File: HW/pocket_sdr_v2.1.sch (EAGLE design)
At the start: 75 parts, among them J1 PIN HEADER 2MM 2P, J2 PIN HEADER 2MM 2P, J3 USB MICRO B RECEPTACLE SMT, J4 SMA JACK EDGE MNT, U1 MAX2771, U2 MAX2771, U3 EZ-USB FX2LP CY7C6813A-56TXC, U4 AT24C128C 8-TSSOP, U5 LDO 3.3V 500mA SOT23-5

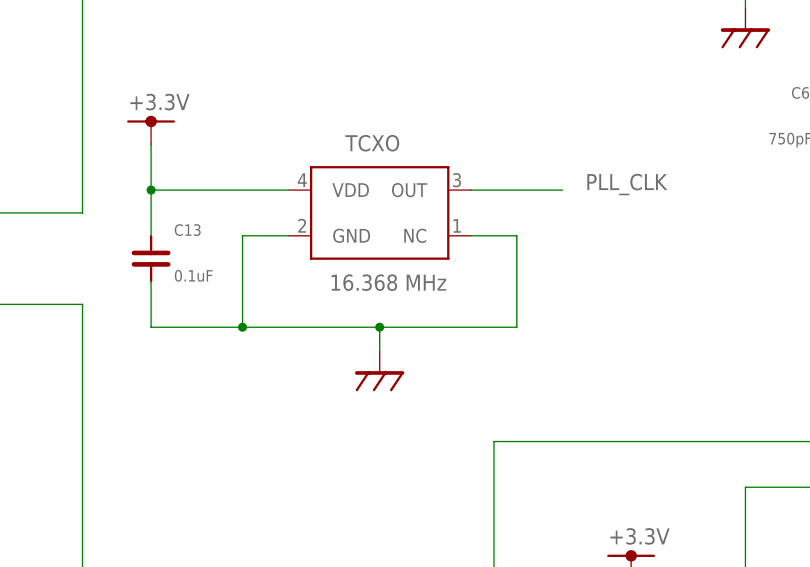
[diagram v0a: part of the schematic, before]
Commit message: TCXO 16.368 -> 24.000 MHz
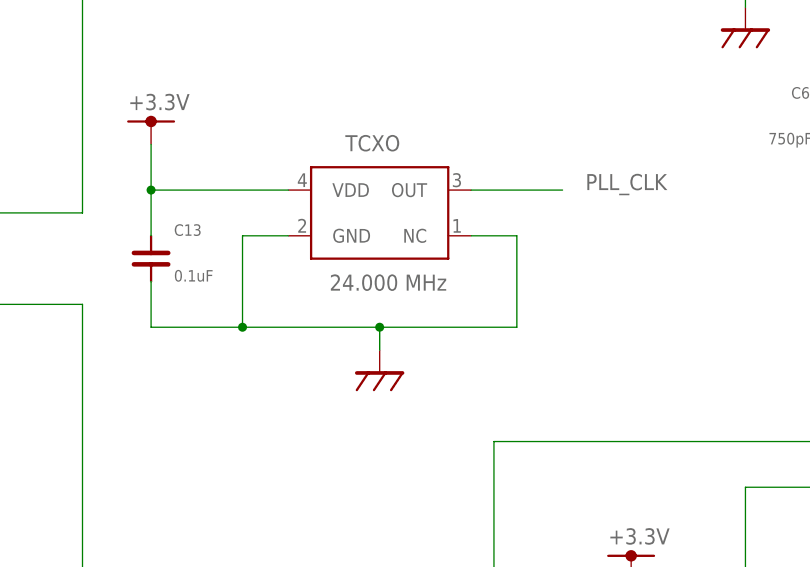
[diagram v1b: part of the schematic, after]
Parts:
- TCXO: value 16.368 MHz -> 24.000 MHz
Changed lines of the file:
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@@
 <part name="U$31" library="power" deviceset="GND" device=""/>
 <part name="U$32" library="power" deviceset="+3.3V" device=""/>
-<part name="TCXO" library="ttaka_misc" deviceset="TCXO" device="" value="16.368 MHz"/>
+<part name="TCXO" library="ttaka_misc" deviceset="TCXO" device="" value="24.000 MHz"/>
 <part name="U$7" library="power" deviceset="GND" device=""/>
 <part name="C13" library="ttaka_desc" deviceset="C1005" device="" value="0.1uF"/>
